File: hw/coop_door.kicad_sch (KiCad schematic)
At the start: 53 parts, among them J1 Screw_Terminal_01x02, J2 Screw_Terminal_01x02, J3 Screw_Terminal_01x02, Q1 Q_NMOS_DDGSDD, Q2 IRF4905, Q3 Q_NMOS_DDGSDD, Q4 Q_Dual_NMOS_S1G1D2S2G2D1, Q5 Q_PMOS_DDGSDD, SW1 SW_Push, SW2 SW_DPDT_x2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

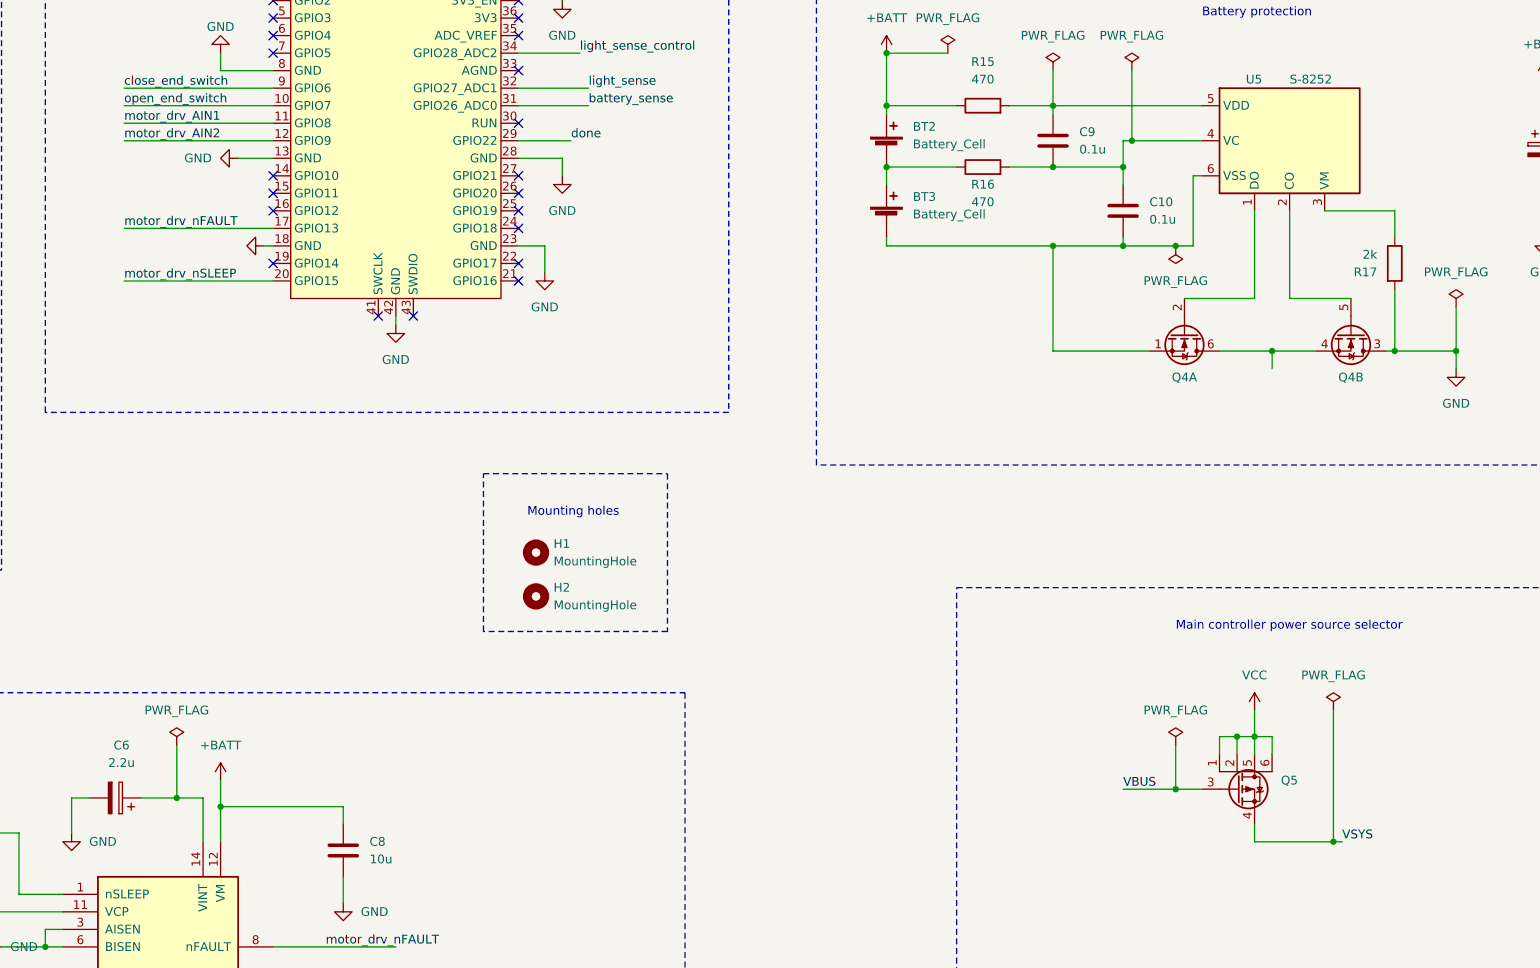
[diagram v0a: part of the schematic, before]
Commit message: Revise PCB dimensions
* Add project specific symbol library
* Change PCB dimensions to fit the housing
* Move some components for the connectors to be easily accessible
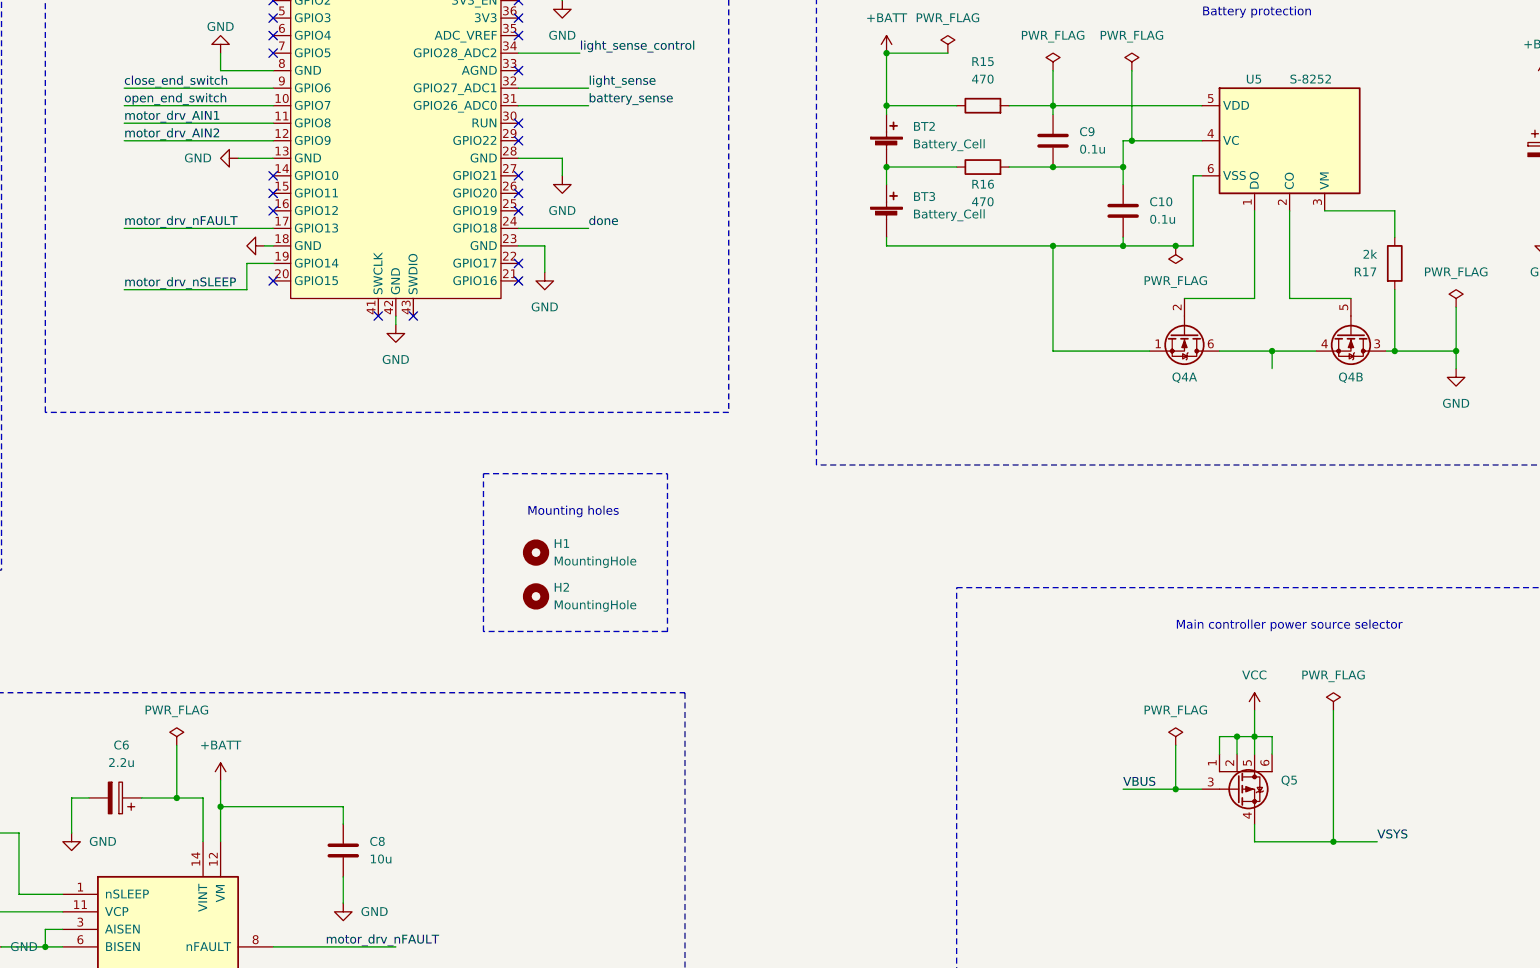
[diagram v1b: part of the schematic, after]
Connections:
- net done: now also U4.24 (GPIO18); no longer U4.29 (GPIO22)
- net motor_drv_nSLEEP: now also U4.19 (GPIO14); no longer U4.20 (GPIO15)

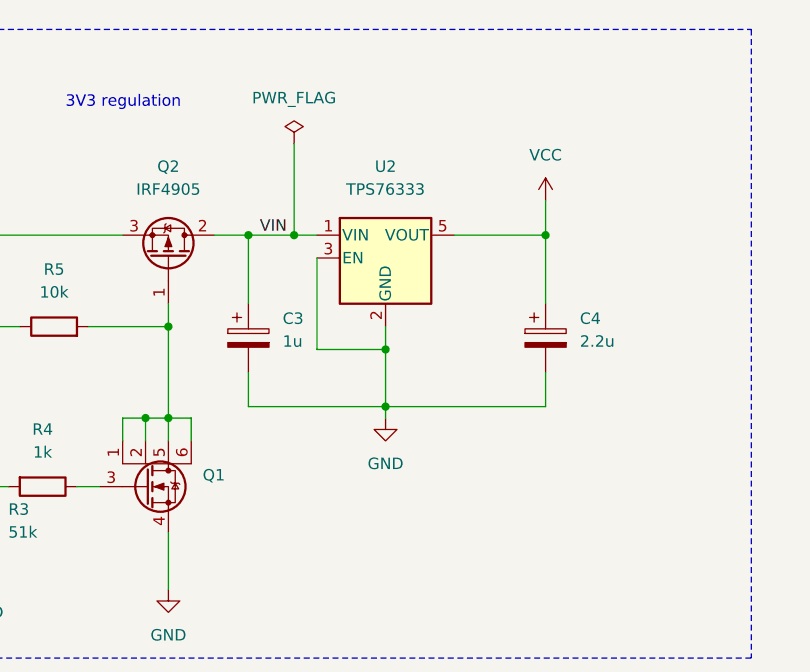
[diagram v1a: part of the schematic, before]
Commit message: V-regulator
Use a correct symbol and package for TPS76633 voltage regulator.
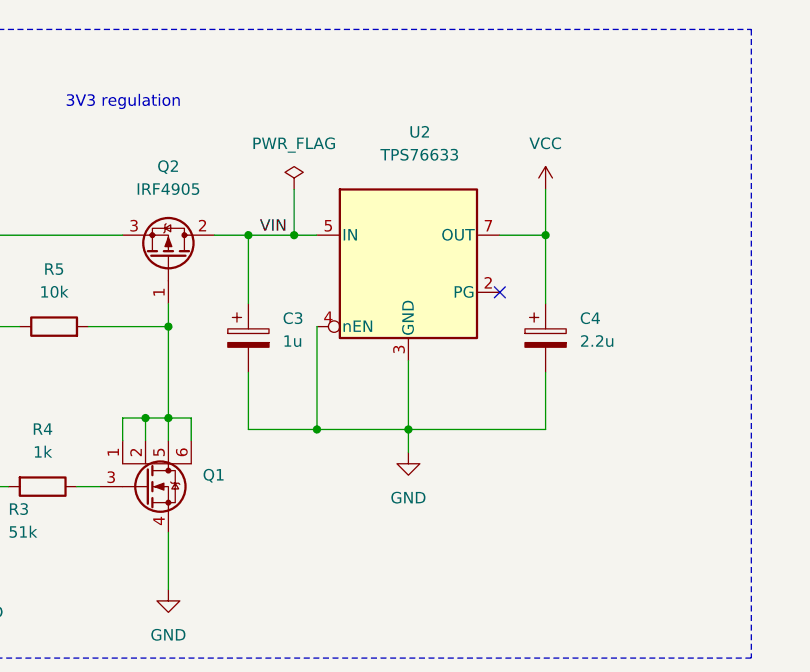
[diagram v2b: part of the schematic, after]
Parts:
- removed U2: TPS76333, Package_TO_SOT_SMD:SOT-23-5, symbol Regulator_Linear:TPS76333
- added U2: TPS76633, Package_SO:SOIC-8-1EP_3.9x4.9mm_P1.27mm_EP2.514x3.2mm, symbol coop_door_library:TPS76633
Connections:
- net GND: now also U2.3 (GND), U2.4 (nEN)
- net VCC: now also U2.7 (OUT), U2.8 (OUT)
- net VIN: now also U2.5 (IN), U2.6 (IN)
- no-connect marks 31 -> 32
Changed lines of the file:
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@@
   (junction (at 73.66 40.64) (diameter 0) (color 0 0 0 0)
   )
-  (junction (at 118.11 53.34) (diameter 0) (color 0 0 0 0)
-  )
   (junction (at 317.5 132.08) (diameter 0) (color 0 0 0 0)
   )
@@
   (junction (at 335.28 143.51) (diameter 0) (color 0 0 0 0)
   )
-  (junction (at 118.11 59.69) (diameter 0) (color 0 0 0 0)
-  )
   (junction (at 135.89 144.78) (diameter 0) (color 0 0 0 0)
   )
@@
   (junction (at 50.8 228.6) (diameter 0) (color 0 0 0 0)
   )
+  (junction (at 135.89 40.64) (diameter 0) (color 0 0 0 0)
+  )
   (junction (at 58.42 107.95) (diameter 0) (color 0 0 0 0)
   )
@@
   (junction (at 107.95 40.64) (diameter 0) (color 0 0 0 0)
   )
+  (junction (at 120.65 62.23) (diameter 0) (color 0 0 0 0)
+  )
   (junction (at 375.92 158.75) (diameter 0) (color 0 0 0 0)
   )
@@
   (junction (at 190.5 223.52) (diameter 0) (color 0 0 0 0)
   )
+  (junction (at 110.49 62.23) (diameter 0) (color 0 0 0 0)
+  )
   (junction (at 295.91 45.72) (diameter 0) (color 0 0 0 0)
   )
@@
   (junction (at 346.71 214.63) (diameter 0) (color 0 0 0 0)
   )
-  (junction (at 135.89 40.64) (diameter 0) (color 0 0 0 0)
-  )
   (junction (at 133.35 228.6) (diameter 0) (color 0 0 0 0)
   )
@@
   (no_connect (at 204.47 135.89))
   (no_connect (at 55.88 55.88))
+  (no_connect (at 130.81 46.99))
   (no_connect (at 55.88 60.96))
   (no_connect (at 204.47 133.35))
@@
     (stroke (width 0) (type default))
   )
-  (wire (pts (xy 41.91 228.6) (xy 50.8 228.6))
+  (wire (pts (xy 135.89 35.56) (xy 135.89 40.64))
     (stroke (width 0) (type default))
   )
-  (wire (pts (xy 196.85 118.11) (xy 204.47 118.11))
+  (wire (pts (xy 41.91 228.6) (xy 50.8 228.6))
     (stroke (width 0) (type default))
   )
-  (wire (pts (xy 135.89 48.26) (xy 135.89 40.64))
+  (wire (pts (xy 196.85 118.11) (xy 204.47 118.11))
     (stroke (width 0) (type default))
   )
@@
     (stroke (width 0) (type default))
   )
-  (wire (pts (xy 135.89 55.88) (xy 135.89 59.69))
+  (wire (pts (xy 135.89 55.88) (xy 135.89 62.23))
     (stroke (width 0) (type default))
   )
@@
     (stroke (width 0) (type default))
   )
+  (wire (pts (xy 130.81 40.64) (xy 135.89 40.64))
+    (stroke (width 0) (type default))
+  )
   (wire (pts (xy 358.14 210.82) (xy 358.14 229.87))
     (stroke (width 0) (type default))
@@
     (stroke (width 0) (type default))
   )
-  (wire (pts (xy 107.95 30.48) (xy 107.95 40.64))
-    (stroke (width 0) (type default))
-  )
-  (wire (pts (xy 110.49 43.18) (xy 110.49 53.34))
+  (wire (pts (xy 107.95 35.56) (xy 107.95 40.64))
     (stroke (width 0) (type default))
   )
@@
     (stroke (width 0) (type default))
   )
+  (wire (pts (xy 120.65 62.23) (xy 135.89 62.23))
+    (stroke (width 0) (type default))
+  )
   (wire (pts (xy 118.11 138.43) (xy 118.11 139.7))
     (stroke (width 0) (type default))
@@
     (stroke (width 0) (type default))
   )
+  (wire (pts (xy 120.65 54.61) (xy 120.65 62.23))
+    (stroke (width 0) (type default))
+  )
   (wire (pts (xy 133.35 240.03) (xy 133.35 246.38))
     (stroke (width 0) (type default))
@@
     (stroke (width 0) (type default))
   )
-  (wire (pts (xy 118.11 60.96) (xy 118.11 59.69))
-    (stroke (width 0) (type default))
-  )
   (wire (pts (xy 88.9 119.38) (xy 99.06 119.38))
     (stroke (width 0) (type default))
@@
     (stroke (width 0) (type default))
   )
-  (wire (pts (xy 135.89 36.83) (xy 135.89 40.64))
-    (stroke (width 0) (type default))
-  )
   (wire (pts (xy 327.66 132.08) (xy 327.66 134.62))
     (stroke (width 0) (type default))
@@
     (stroke (width 0) (type default))
   )
+  (wire (pts (xy 120.65 62.23) (xy 120.65 64.77))
+    (stroke (width 0) (type default))
+  )
   (wire (pts (xy 388.62 133.35) (xy 388.62 142.24))
     (stroke (width 0) (type default))
@@
     (stroke (width 0) (type default))
   )
-  (wire (pts (xy 107.95 40.64) (xy 110.49 40.64))
+  (wire (pts (xy 135.89 40.64) (xy 135.89 48.26))
     (stroke (width 0) (type default))
   )
-  (wire (pts (xy 125.73 40.64) (xy 135.89 40.64))
+  (wire (pts (xy 107.95 40.64) (xy 110.49 40.64))
     (stroke (width 0) (type default))
   )
@@
     (stroke (width 0) (type default))
   )
-  (wire (pts (xy 102.87 59.69) (xy 118.11 59.69))
+  (wire (pts (xy 102.87 62.23) (xy 110.49 62.23))
     (stroke (width 0) (type default))
   )
@@
     (stroke (width 0) (type default))
   )
-  (wire (pts (xy 118.11 53.34) (xy 118.11 50.8))
-    (stroke (width 0) (type default))
-  )
   (wire (pts (xy 327.66 128.27) (xy 327.66 132.08))
     (stroke (width 0) (type default))
@@
     (stroke (width 0) (type default))
   )
-  (wire (pts (xy 118.11 59.69) (xy 135.89 59.69))
+  (wire (pts (xy 110.49 62.23) (xy 120.65 62.23))
     (stroke (width 0) (type default))
   )
@@
     (stroke (width 0) (type default))
   )
-  (wire (pts (xy 102.87 55.88) (xy 102.87 59.69))
+  (wire (pts (xy 102.87 55.88) (xy 102.87 62.23))
     (stroke (width 0) (type default))
   )
@@
     (stroke (width 0) (type default))
   )
-  (wire (pts (xy 110.49 53.34) (xy 118.11 53.34))
+  (wire (pts (xy 110.49 50.8) (xy 110.49 62.23))
     (stroke (width 0) (type default))
   )
@@
     (stroke (width 0) (type default))
   )
-  (wire (pts (xy 118.11 59.69) (xy 118.11 53.34))
-    (stroke (width 0) (type default))
-  )
   (wire (pts (xy 93.98 50.8) (xy 93.98 60.96))
     (stroke (width 0) (type default))
@@
     )
   )
-  (symbol (lib_name "GND_7") (lib_id "power:GND") (at 118.11 60.96 0) (unit 1)
+  (symbol (lib_name "GND_7") (lib_id "power:GND") (at 120.65 64.77 0) (unit 1)
     (in_bom yes) (on_board yes) (dnp no) (fields_autoplaced)
-    (property "Reference" "#PWR011" (at 118.11 67.31 0)
+    (property "Reference" "#PWR011" (at 120.65 71.12 0)
       (effects (font (size 1.27 1.27)) hide)
     )
-    (property "Value" "GND" (at 118.11 66.04 0)
+    (property "Value" "GND" (at 120.65 69.85 0)
       (effects (font (size 1.27 1.27)))
     )
-    (property "Footprint" "" (at 118.11 60.96 0)
+    (property "Footprint" "" (at 120.65 64.77 0)
       (effects (font (size 1.27 1.27)) hide)
     )
-    (property "Datasheet" "" (at 118.11 60.96 0)
+    (property "Datasheet" "" (at 120.65 64.77 0)
       (effects (font (size 1.27 1.27)) hide)
     )
@@
     )
   )
-  (symbol (lib_id "Regulator_Linear:TPS76333") (at 118.11 43.18 0) (unit 1)
-    (in_bom yes) (on_board yes) (dnp no) (fields_autoplaced)
-    (property "Reference" "U2" (at 118.11 33.02 0)
-      (effects (font (size 1.27 1.27)))
-    )
-    (property "Value" "TPS76333" (at 118.11 35.56 0)
-      (effects (font (size 1.27 1.27)))
-    )
-    (property "Footprint" "Package_TO_SOT_SMD:SOT-23-5" (at 118.11 34.925 0)
-      (effects (font (size 1.27 1.27) italic) hide)
-    )
-    (property "Datasheet" "http://www.ti.com/lit/ds/symlink/tps763.pdf" (at 118.11 43.18 0)
-      (effects (font (size 1.27 1.27)) hide)
-    )
-    (pin "1")
-    (pin "2")
-    (pin "3")
-    (pin "4")
-    (pin "5")
-    (instances
-      (project "coop_door"
-        (path "/9538e4ed-27e6-4c37-b989-9859dc0d49e8"
-          (reference "U2") (unit 1)
-        )
-      )
-    )
-  )
   (symbol (lib_id "Device:R") (at 127 144.78 270) (unit 1)
     (in_bom yes) (on_board yes) (dnp no)
@@
     )
   )
+  (symbol (lib_id "coop_door_library:TPS76633") (at 120.65 40.64 0) (unit 1)
+    (in_bom yes) (on_board yes) (dnp no) (fields_autoplaced)
+    (property "Reference" "U2" (at 121.92 29.21 0)
+      (effects (font (size 1.27 1.27)))
+    )
+    (property "Value" "TPS76633" (at 121.92 31.75 0)
+      (effects (font (size 1.27 1.27)))
+    )
+    (property "Footprint" "Package_SO:SOIC-8-1EP_3.9x4.9mm_P1.27mm_EP2.514x3.2mm" (at 124.46 26.67 0)
+      (effects (font (size 1.27 1.27) italic) hide)
+    )
+    (property "Datasheet" "https://www.ti.com/lit/ds/symlink/tps766.pdf" (at 124.46 52.07 0)
+      (effects (font (size 1.27 1.27)) hide)
+    )
+    (pin "8")
+    (pin "6")
+    (pin "7")
+    (pin "5")
+    (pin "1")
+    (pin "2")
+    (pin "3")
+    (pin "4")
+    (instances
+      (project "coop_door"
+        (path "/9538e4ed-27e6-4c37-b989-9859dc0d49e8"
+          (reference "U2") (unit 1)
+        )
+      )
+    )
+  )
   (symbol (lib_id "Device:R") (at 307.34 132.08 90) (unit 1)
     (in_bom yes) (on_board yes) (dnp no)
@@
     )
   )
-  (symbol (lib_name "VCC_1") (lib_id "power:VCC") (at 135.89 36.83 0) (unit 1)
+  (symbol (lib_name "VCC_1") (lib_id "power:VCC") (at 135.89 35.56 0) (unit 1)
     (in_bom yes) (on_board yes) (dnp no) (fields_autoplaced)
-    (property "Reference" "#PWR013" (at 135.89 40.64 0)
+    (property "Reference" "#PWR013" (at 135.89 39.37 0)
       (effects (font (size 1.27 1.27)) hide)
     )
-    (property "Value" "VCC" (at 135.89 31.75 0)
+    (property "Value" "VCC" (at 135.89 30.48 0)
       (effects (font (size 1.27 1.27)))
     )
-    (property "Footprint" "" (at 135.89 36.83 0)
+    (property "Footprint" "" (at 135.89 35.56 0)
       (effects (font (size 1.27 1.27)) hide)
     )
-    (property "Datasheet" "" (at 135.89 36.83 0)
+    (property "Datasheet" "" (at 135.89 35.56 0)
       (effects (font (size 1.27 1.27)) hide)
     )
@@
     )
   )
-  (symbol (lib_name "PWR_FLAG_7") (lib_id "power:PWR_FLAG") (at 107.95 30.48 0) (unit 1)
+  (symbol (lib_name "PWR_FLAG_7") (lib_id "power:PWR_FLAG") (at 107.95 35.56 0) (unit 1)
     (in_bom yes) (on_board yes) (dnp no) (fields_autoplaced)
-    (property "Reference" "#FLG02" (at 107.95 28.575 0)
+    (property "Reference" "#FLG02" (at 107.95 33.655 0)
       (effects (font (size 1.27 1.27)) hide)
     )
-    (property "Value" "PWR_FLAG" (at 107.95 25.4 0)
+    (property "Value" "PWR_FLAG" (at 107.95 30.48 0)
       (effects (font (size 1.27 1.27)))
     )
-    (property "Footprint" "" (at 107.95 30.48 0)
+    (property "Footprint" "" (at 107.95 35.56 0)
       (effects (font (size 1.27 1.27)) hide)
     )
-    (property "Datasheet" "~" (at 107.95 30.48 0)
+    (property "Datasheet" "~" (at 107.95 35.56 0)
       (effects (font (size 1.27 1.27)) hide)
     )
